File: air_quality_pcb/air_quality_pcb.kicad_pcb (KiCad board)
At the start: 2 copper layers, 75 x 70 mm, 23 parts, among them IC1 SCD41-D-R2, IC2 SGP41-D-R4, J1 Conn_01x02, J2 52435-2871, U1 XIAO-ESP32-C6, U2 MQ-6, U3 MQ-6

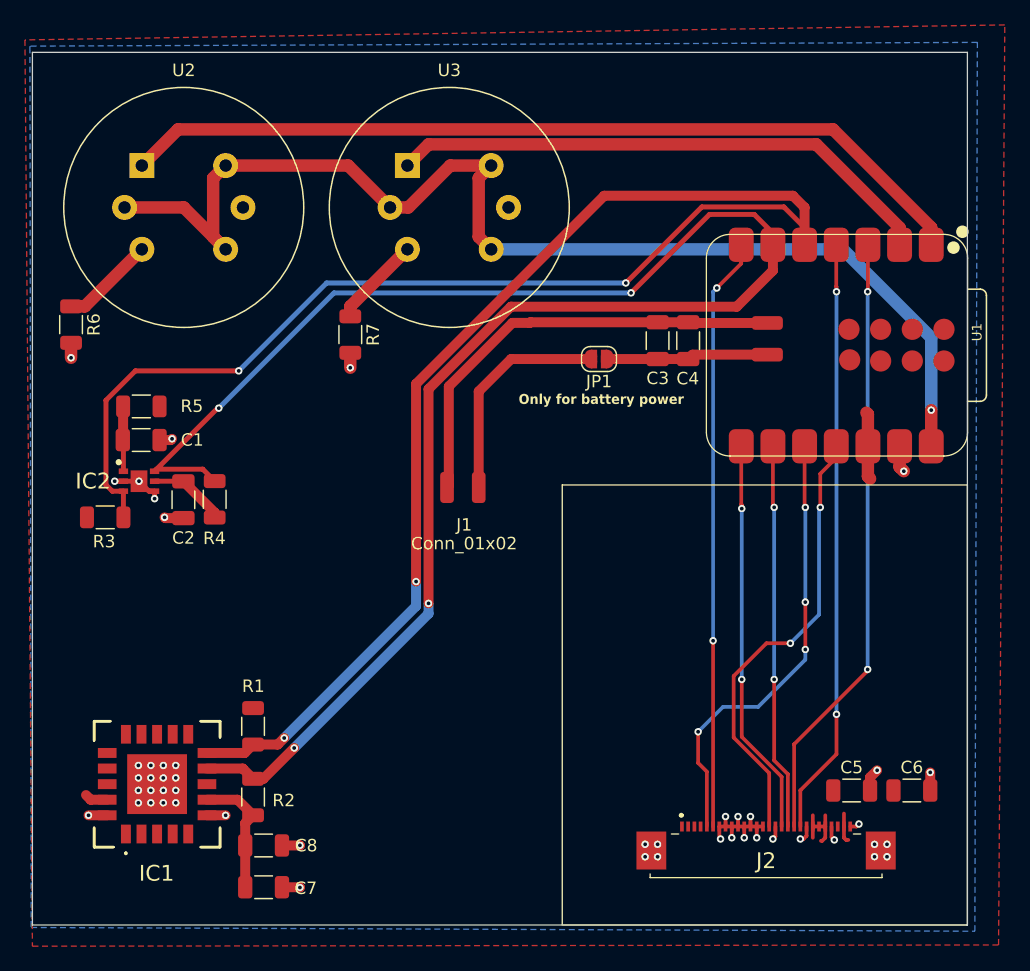
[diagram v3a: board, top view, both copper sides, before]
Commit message: added buck boost for 5v battery powered
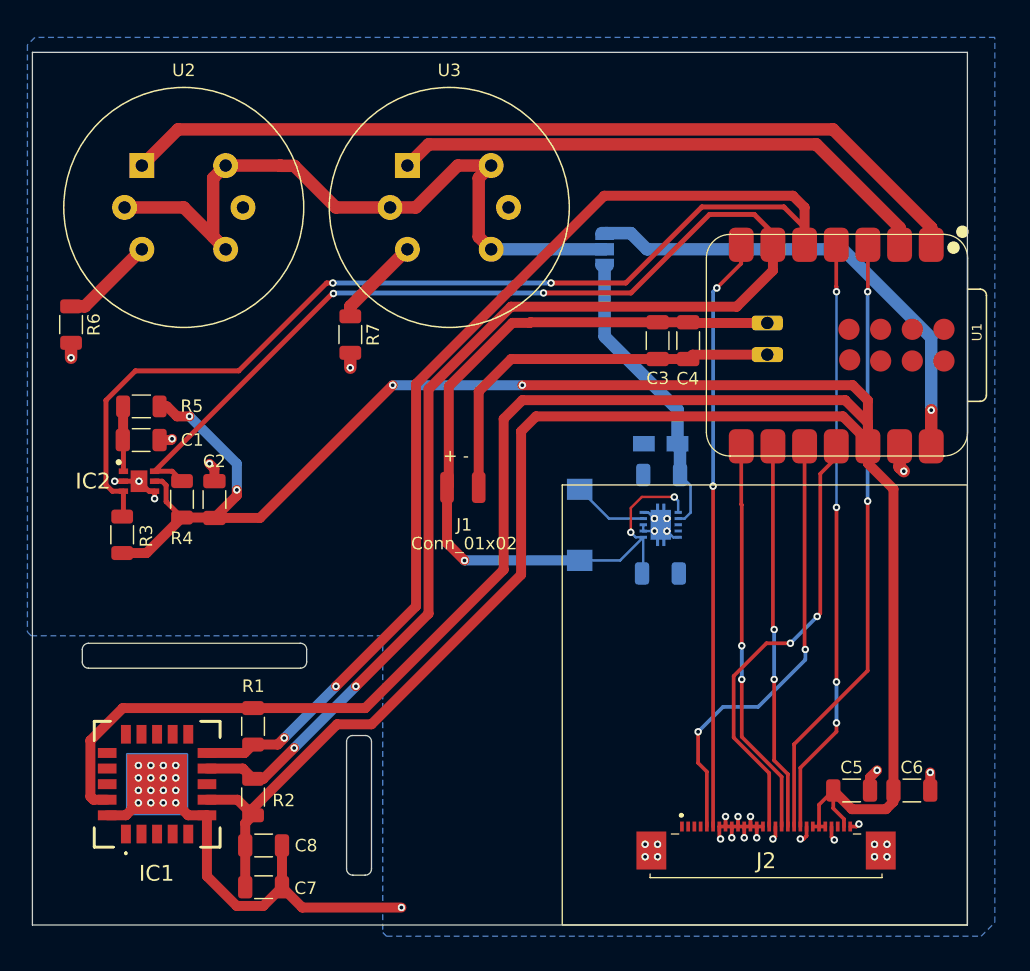
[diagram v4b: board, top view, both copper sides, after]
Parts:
- removed JP1: Jumper_2_Open, Jumper:SolderJumper-2_P1.3mm_Open_RoundedPad1.0x1.5mm
- added C10: 47uF, project_extras:CAPPM3216X180N, B.Cu at (90.5, 92.3)
- added C11: 10uF, Capacitor_SMD:C_1206_3216Metric, B.Cu at (90.5, 102.7)
- added C9: 2,2uF, Capacitor_SMD:C_1206_3216Metric, B.Cu at (90.6, 94.8)
- added IC3: TPS61027DRCR, project_extras:TPS74901DRCR, B.Cu at (90.5, 98.8)
- added JP2: SolderJumper_3_Open, Jumper:SolderJumper-3_P1.3mm_Open_RoundedPad1.0x1.5mm_NumberLabels, B.Cu at (86.0, 76.7)
- added L1: 6,8uH, project_extras:INDPM6363X300N, B.Cu at (84.0, 98.8)
- moved R4 2.62 mm to (52.1, 96.8)
- moved C2 2.49 mm to (54.7, 96.8), turned to 90 degrees
- moved R3 1.95 mm to (47.3, 99.6), turned to 90 degrees
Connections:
- C1 pad 2: GND -> -BATT
- C2 pad 2: GND -> -BATT
- C3 pad 2: Net-(JP1-A) -> -BATT
- C4 pad 2: Net-(JP1-A) -> -BATT
- C5 pad 2: GND -> -BATT
- C6 pad 2: GND -> -BATT
- C7 pad 1: GND -> -BATT
- C8 pad 1: GND -> -BATT
- IC1 pad 20: GND -> -BATT
- IC1 pad 21: GND -> -BATT
- IC1 pad 6: GND -> -BATT
- IC2 pad 2: GND -> -BATT
- IC2 pad 4: GND -> -BATT
- IC2 pad 7: GND -> -BATT
- J2 pad 10: GND -> -BATT
- J2 pad 11: GND -> -BATT
- J2 pad 12: GND -> -BATT
- J2 pad 13: GND -> -BATT
- J2 pad 14: GND -> -BATT
- J2 pad 16: GND -> -BATT
- J2 pad 21: GND -> -BATT
- J2 pad 25: GND -> -BATT
- J2 pad 28: GND -> -BATT
- J2 pad 7: GND -> -BATT
- J2 pad 8: GND -> -BATT
- J2 pad 9: GND -> -BATT
- J2 pad MP1: GND -> -BATT
- J2 pad MP2: GND -> -BATT
- R6 pad 2: GND -> -BATT
- R7 pad 2: GND -> -BATT
- U1 pad 13: GND -> -BATT
- U1 pad 16: Net-(JP1-A) -> -BATT
- U2 pad 2: +5V -> MQ-x
- U2 pad 4: +5V -> MQ-x
- U2 pad 5: GND -> -BATT
- U2 pad 6: +5V -> MQ-x
- U3 pad 2: +5V -> MQ-x
- U3 pad 4: +5V -> MQ-x
- U3 pad 5: GND -> -BATT
- U3 pad 6: +5V -> MQ-x
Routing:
- net +3V3: track 31.2 -> 300.1 mm, vias 0 -> 4
- net -BATT: track 17.8 -> 102.7 mm, vias 0 -> 50
- net MQ-x: track 0.00 -> 57.8 mm
- net +5V: track 95.6 -> 38.4 mm
- net GND: track 34.5 -> 0.00 mm, vias 49 -> 0
- net +BATT: track 35.9 -> 68.7 mm, vias 0 -> 3
- net 5V: track 0.00 -> 23.9 mm
- net Net-(JP1-A): track 13.0 -> 0.00 mm
- net Net-(IC3-SW): track 0.00 -> 6.07 mm
- net SCL: track 140.2 -> 137.5 mm
- net SDOX: vias 4 -> 2
- net RESX: vias 2 -> 4
- added copper zone on B.Cu, net -BATT
- removed copper zone on F.Cu, net +3V3
- removed copper zone on B.Cu, net GND
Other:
- outline, holes or cut-outs redrawn
- board text added: "+ -"
- board text added: "1 -> ESP 3 -> BATT"
- board text removed: "Only for battery power"

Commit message: added buzzer
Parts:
- added BZ1: Buzzer, Buzzer_Beeper:Buzzer_12x9.5RM7.6, F.Cu at (85.4, 64.2)
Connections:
- J2 pad 6: TE -> unconnected-(J2-Pad6)
- U1 pad 7: TE -> BUZZ
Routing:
- net TE: track 47.6 -> 0.00 mm, vias 2 -> 0
- net BUZZ: track 0.00 -> 17.2 mm, vias 0 -> 1
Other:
- board size 75 x 70 mm -> 75 x 75 mm
- board text added: "+"

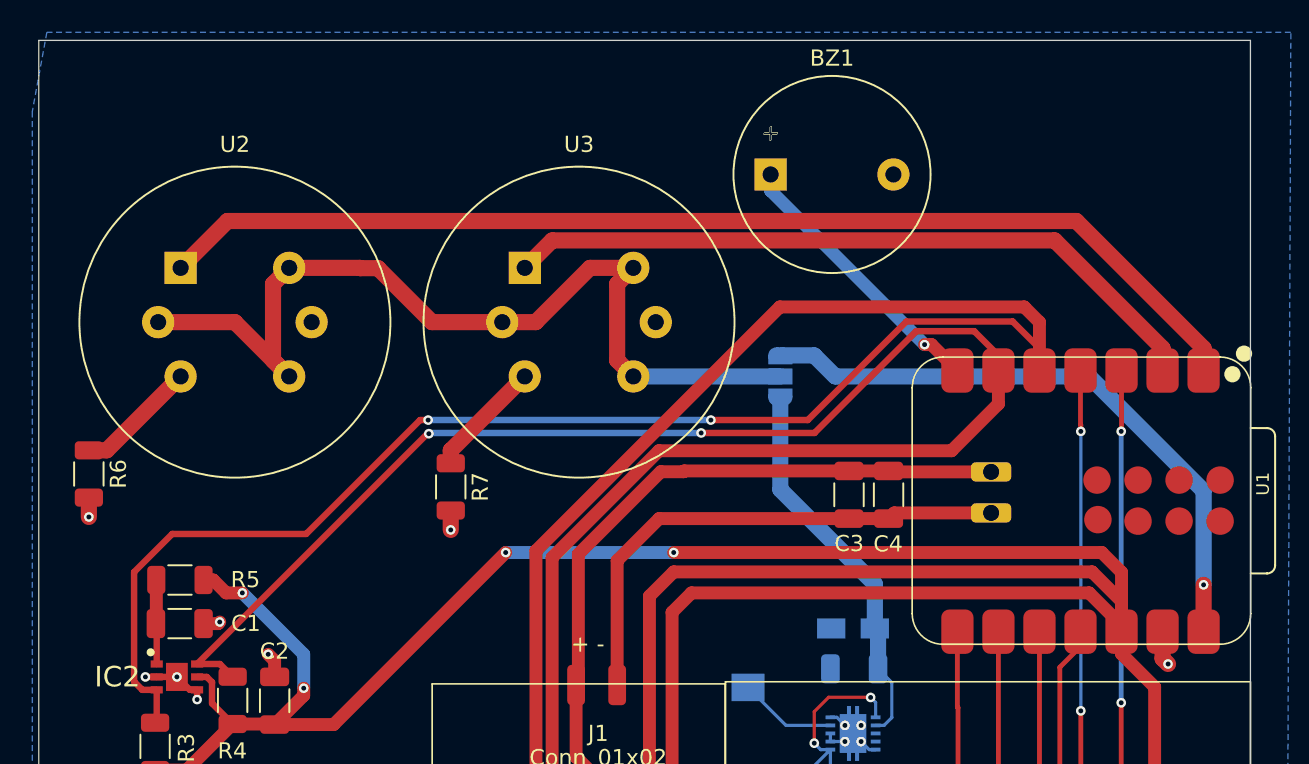
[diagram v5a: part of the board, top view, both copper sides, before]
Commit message: fixed buzzer and MQ-x sensors placement
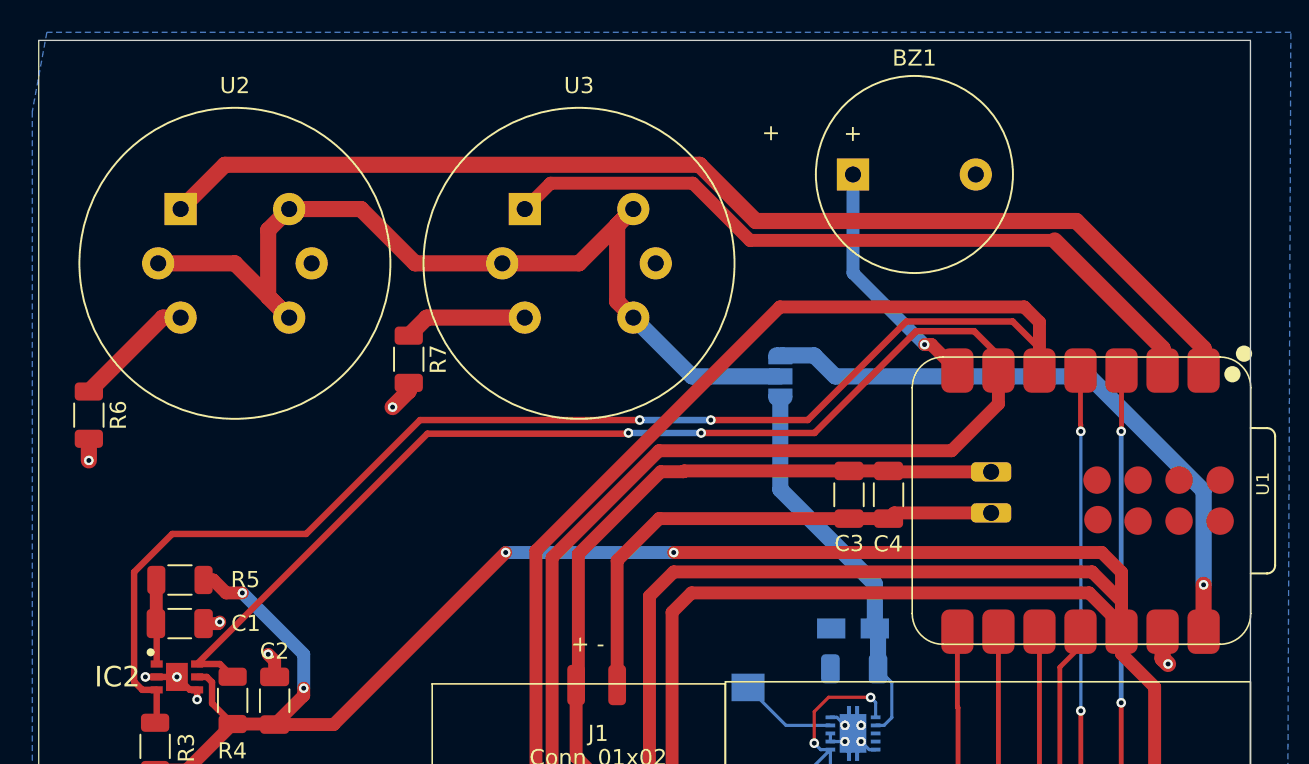
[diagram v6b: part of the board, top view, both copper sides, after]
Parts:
- moved R7 8.32 mm to (63.0, 75.6)
- moved BZ1 5.10 mm to (90.5, 64.2)
- moved R6 3.64 mm to (43.2, 79.1)
- moved U2 3.64 mm to (48.9, 66.3)
- moved U3 3.64 mm to (70.2, 66.3)
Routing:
- net BUZZ: track 17.2 -> 15.1 mm
- net MQ-x: track 57.8 -> 59.5 mm
- net A1: track 44.3 -> 45.8 mm
- net A0: track 69.2 -> 70.5 mm
- net -BATT: track 102.7 -> 103.5 mm
